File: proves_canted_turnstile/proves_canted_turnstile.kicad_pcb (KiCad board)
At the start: 4 copper layers, 100 x 100 mm, 23 parts, among them J1 Conn_Coaxial, J2 Conn_02x02_Counter_Clockwise, U1 QBA-07+, U2 QBA-07+, U3 QBA-07+

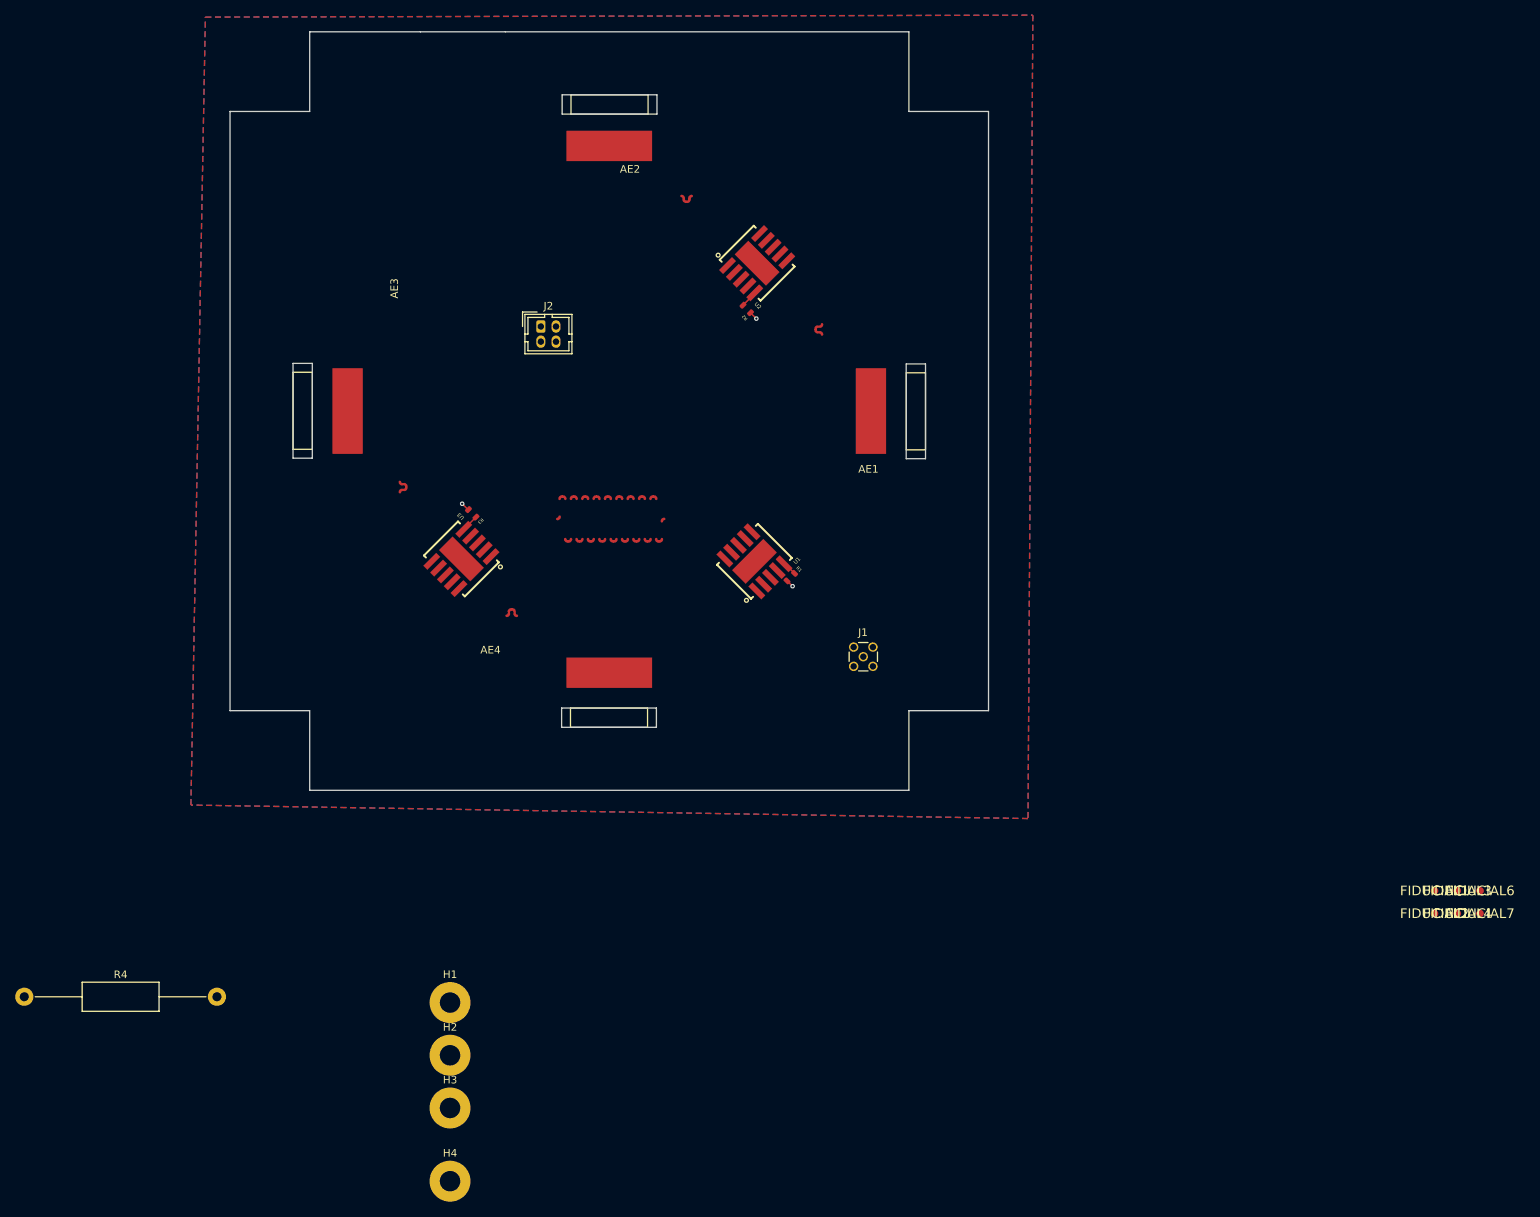
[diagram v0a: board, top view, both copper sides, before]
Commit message: placement of fiducials
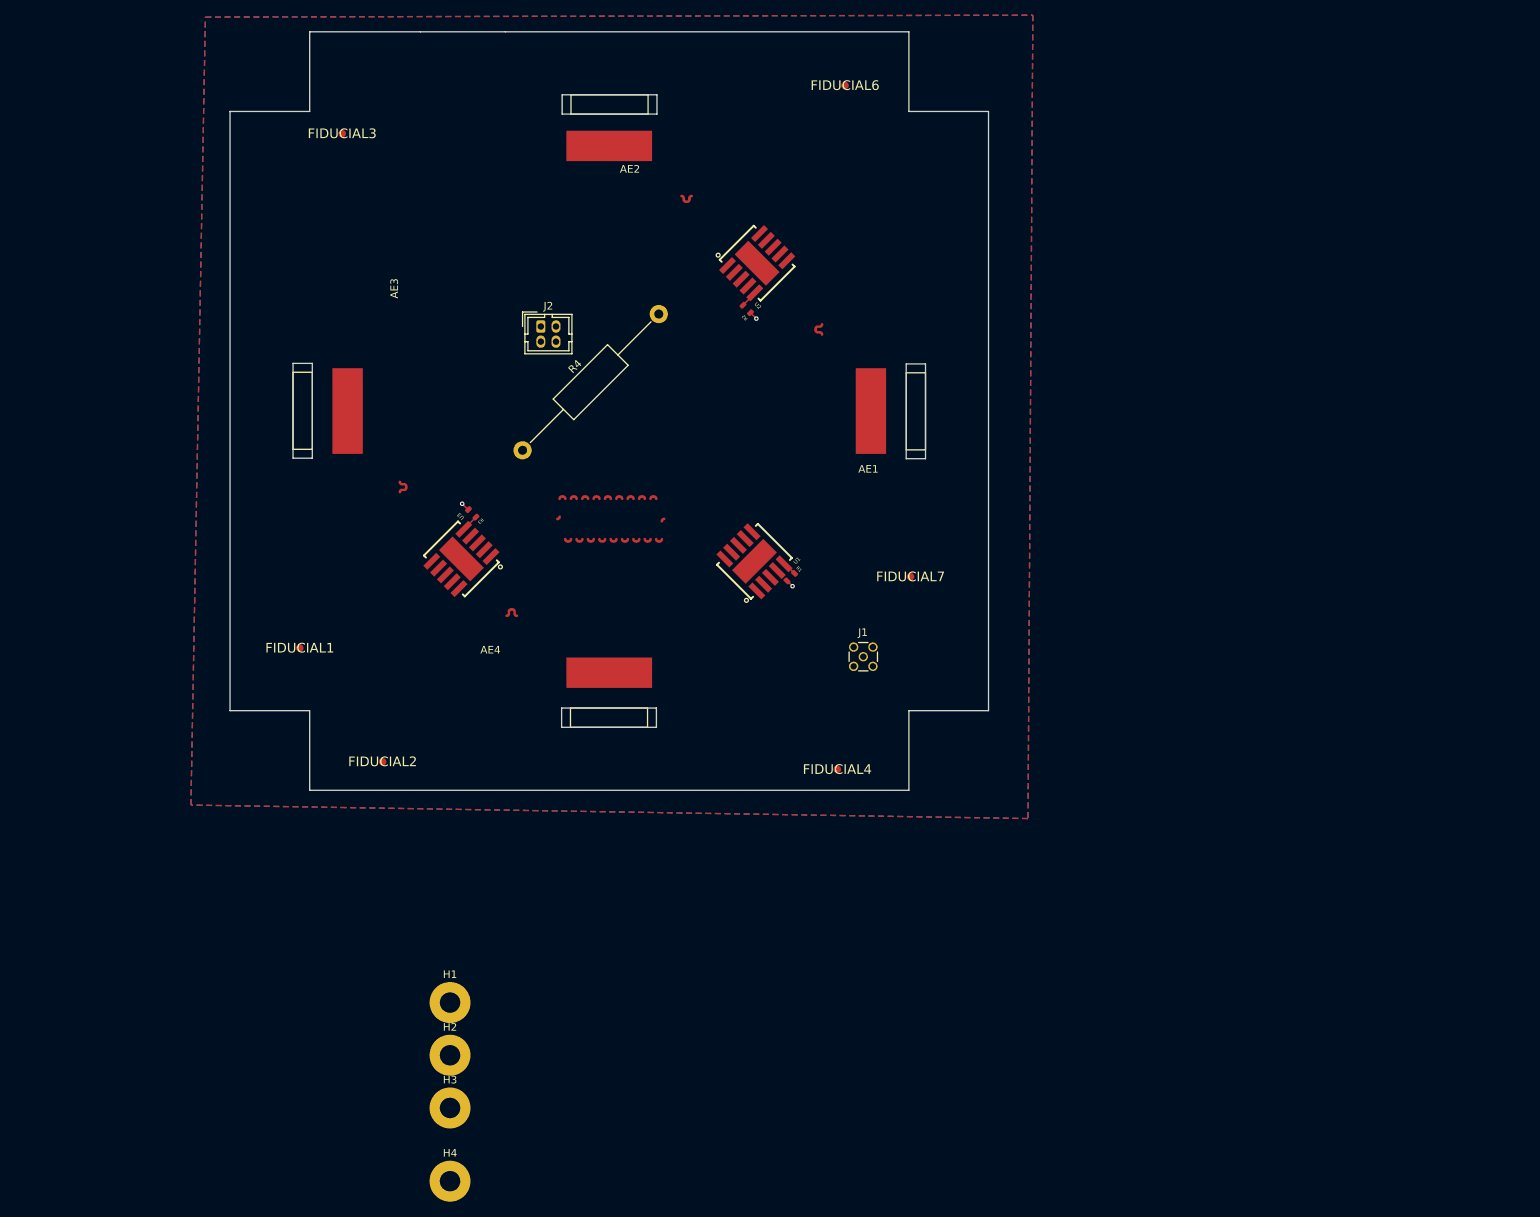
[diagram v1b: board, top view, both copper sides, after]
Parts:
- moved FIDUCIAL3 177.7 mm to (108.5, 46.0)
- moved FIDUCIAL1 153.0 mm to (102.9, 113.8)
- moved FIDUCIAL2 140.1 mm to (113.8, 128.8)
- moved FIDUCIAL6 135.2 mm to (174.8, 39.6)
- moved R4 97.5 mm to (132.2, 87.7), turned to 45 degrees
- moved FIDUCIAL7 87.2 mm to (183.4, 104.4)
- moved FIDUCIAL4 83.9 mm to (173.7, 129.8)
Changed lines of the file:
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@@
 	(footprint "plusz-end-card-with-turnstile-mezzanine-eagle-import:FIDUCIAL-1.0X2.0"
 		(layer "F.Cu")
-		(at 252.476 148.796)
+		(at 113.792 128.778)
 		(descr "Moderate Fiducial, 1.0 mm diameter with 2 mm mask clearance")
 		(property "Reference" "FIDUCIAL2"
@@
 	(footprint "plusz-end-card-with-turnstile-mezzanine-eagle-import:FIDUCIAL-1.0X2.0"
 		(layer "F.Cu")
-		(at 252.476 145.796)
+		(at 102.87 113.792)
 		(descr "Moderate Fiducial, 1.0 mm diameter with 2 mm mask clearance")
 		(property "Reference" "FIDUCIAL1"
@@
 	(footprint "plusz-end-card-with-turnstile-mezzanine-eagle-import:FIDUCIAL-1.0X2.0"
 		(layer "F.Cu")
-		(at 258.476 145.796)
+		(at 174.752 39.624)
 		(descr "Moderate Fiducial, 1.0 mm diameter with 2 mm mask clearance")
 		(property "Reference" "FIDUCIAL6"
@@
 	(footprint "plusz-end-card-with-turnstile-mezzanine-eagle-import:FIDUCIAL-1.0X2.0"
 		(layer "F.Cu")
-		(at 255.476 148.796)
+		(at 173.736 129.794)
 		(descr "Moderate Fiducial, 1.0 mm diameter with 2 mm mask clearance")
 		(property "Reference" "FIDUCIAL4"
@@
 	(footprint "plusz-end-card-with-turnstile-mezzanine-eagle-import:FIDUCIAL-1.0X2.0"
 		(layer "F.Cu")
-		(at 255.476 145.796)
+		(at 108.458 45.974)
 		(descr "Moderate Fiducial, 1.0 mm diameter with 2 mm mask clearance")
 		(property "Reference" "FIDUCIAL3"
@@
 	(footprint "plusz-end-card-with-turnstile-mezzanine-eagle-import:FIDUCIAL-1.0X2.0"
 		(layer "F.Cu")
-		(at 258.476 148.796)
+		(at 183.388 104.394)
 		(descr "Moderate Fiducial, 1.0 mm diameter with 2 mm mask clearance")
 		(property "Reference" "FIDUCIAL7"
@@
 	(footprint "Resistor_THT:R_Axial_DIN0411_L9.9mm_D3.6mm_P25.40mm_Horizontal"
 		(layer "F.Cu")
-		(at 66.548 159.766)
+		(at 132.243744 87.720256 45)
 		(descr "Resistor, Axial_DIN0411 series, Axial, Horizontal, pin pitch=25.4mm, 1W, length*diameter=9.9*3.6mm^2")
 		(tags "Resistor Axial_DIN0411 series Axial Horizontal pin pitch 25.4mm 1W length 9.9mm diameter 3.6mm")
 		(property "Reference" "R4"
-			(at 12.7 -2.92 0)
+			(at 12.7 -2.92 45)
 			(layer "F.SilkS")
 			(effects
@@
 		)
 		(property "Value" "R_Small_US"
-			(at 12.7 2.92 0)
+			(at 12.7 2.92 45)
 			(layer "F.Fab")
 			(effects
@@
 		)
 		(property "Datasheet" ""
-			(at 0 0 0)
+			(at 0 0 45)
 			(unlocked yes)
 			(layer "F.Fab")
@@
 		)
 		(property "Description" "Resistor, small US symbol"
-			(at 0 0 0)
+			(at 0 0 45)
 			(unlocked yes)
 			(layer "F.Fab")
@@
 		(fp_line
 			(start 7.63 1.92)
-			(end 17.77 1.92)
+			(end 17.77 1.920001)
 			(stroke
 				(width 0.12)
@@
 		)
 		(fp_line
-			(start 17.77 -1.92)
+			(start 17.77 -1.920001)
 			(end 7.63 -1.92)
 			(stroke
@@
 		)
 		(fp_line
-			(start 17.77 1.92)
-			(end 17.77 -1.92)
+			(start 17.77 1.920001)
+			(end 17.77 -1.920001)
 			(stroke
 				(width 0.12)
@@
 		)
 		(fp_line
-			(start 23.96 0)
-			(end 17.77 0)
+			(start 23.959999 0)
+			(end 17.770001 0)
 			(stroke
 				(width 0.12)
@@
 		(fp_line
 			(start 0 0)
-			(end 7.75 0)
+			(end 7.750001 0)
 			(stroke
 				(width 0.1)
@@
 		)
 		(fp_text user "${REFERENCE}"
-			(at 12.7 0 0)
+			(at 12.7 0 45)
 			(layer "F.Fab")
 			(effects
@@
 		)
 		(pad "1" thru_hole circle
-			(at 0 0)
+			(at 0 0 45)
 			(size 2.4 2.4)
 			(drill 1.2)
@@
 		)
 		(pad "2" thru_hole oval
-			(at 25.4 0)
+			(at 25.4 0 45)
 			(size 2.4 2.4)
 			(drill 1.2)

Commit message: placed mounting holes
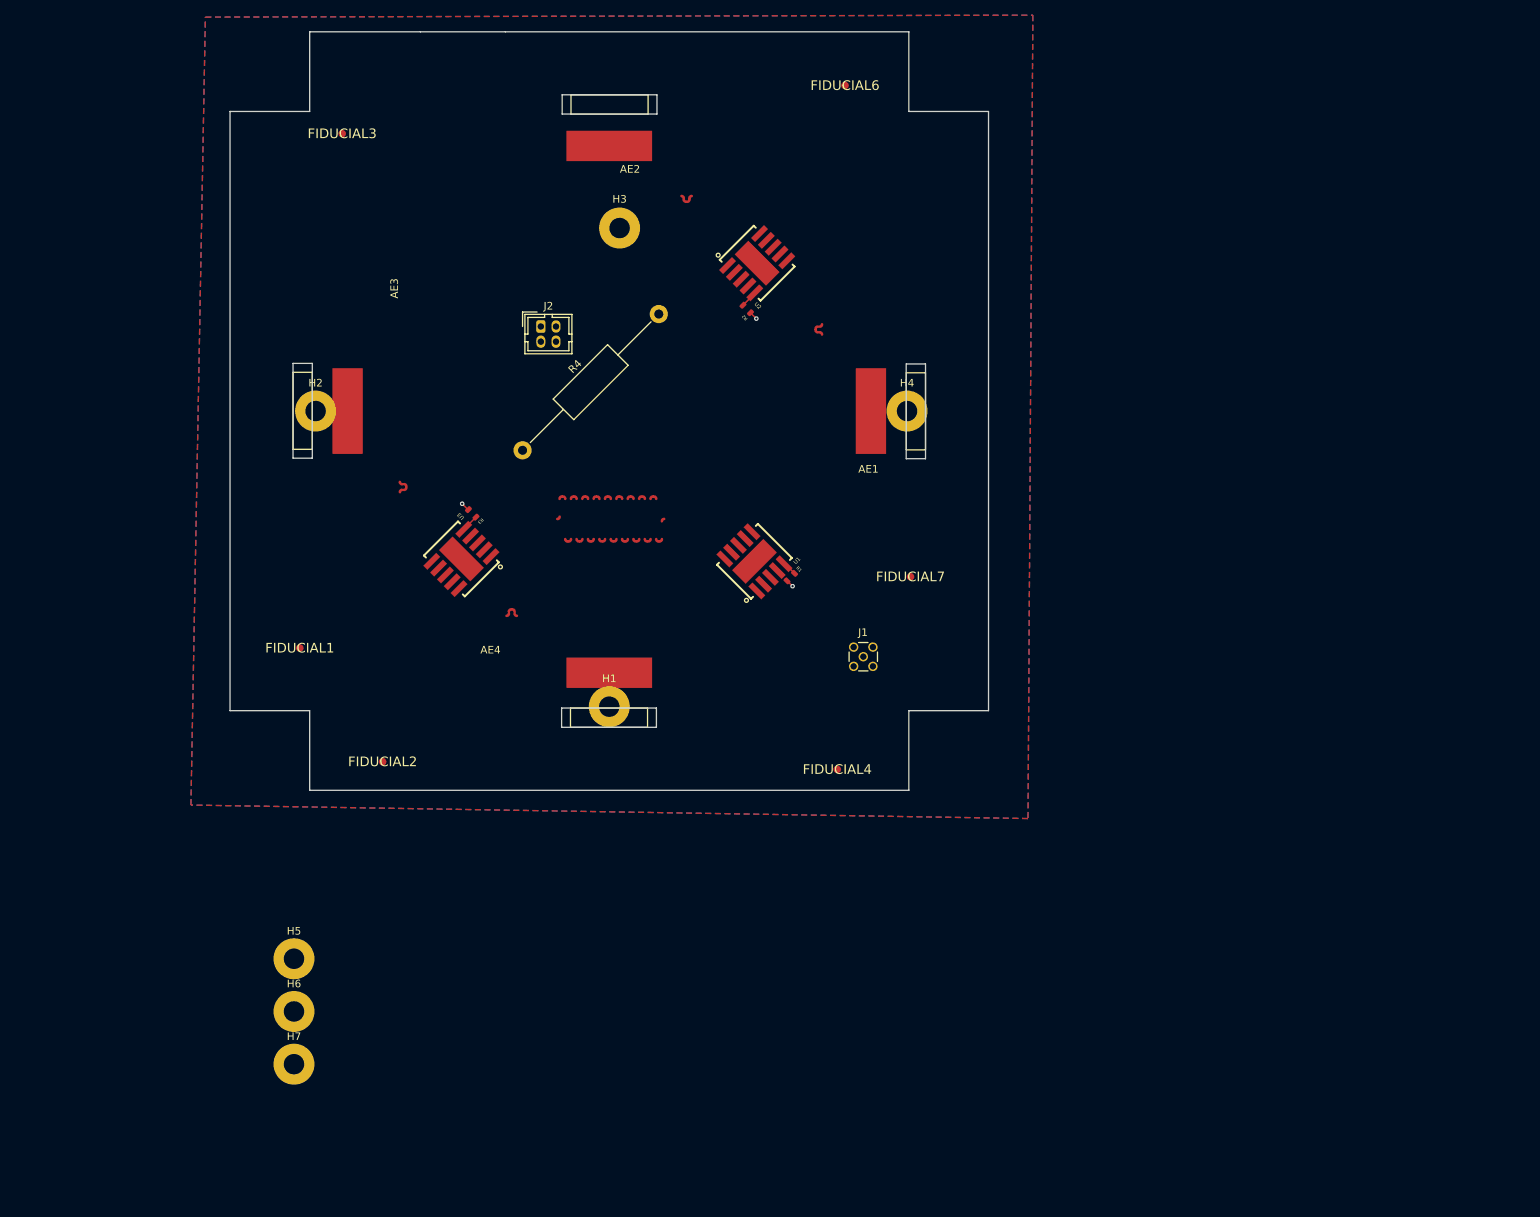
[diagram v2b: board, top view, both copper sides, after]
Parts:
- added H5: MountingHole, MountingHole:MountingHole_2.7mm_M2.5_Pad, F.Cu at (102.1, 154.8)
- added H6: MountingHole, MountingHole:MountingHole_2.7mm_M2.5_Pad, F.Cu at (102.1, 161.7)
- added H7: MountingHole, MountingHole:MountingHole_2.7mm_M2.5_Pad, F.Cu at (102.1, 168.7)
- moved H3 118.1 mm to (145.0, 58.4)
- moved H4 118.1 mm to (182.9, 82.5)
- moved H2 86.8 mm to (105.0, 82.5)
- moved H1 44.3 mm to (143.7, 121.5)

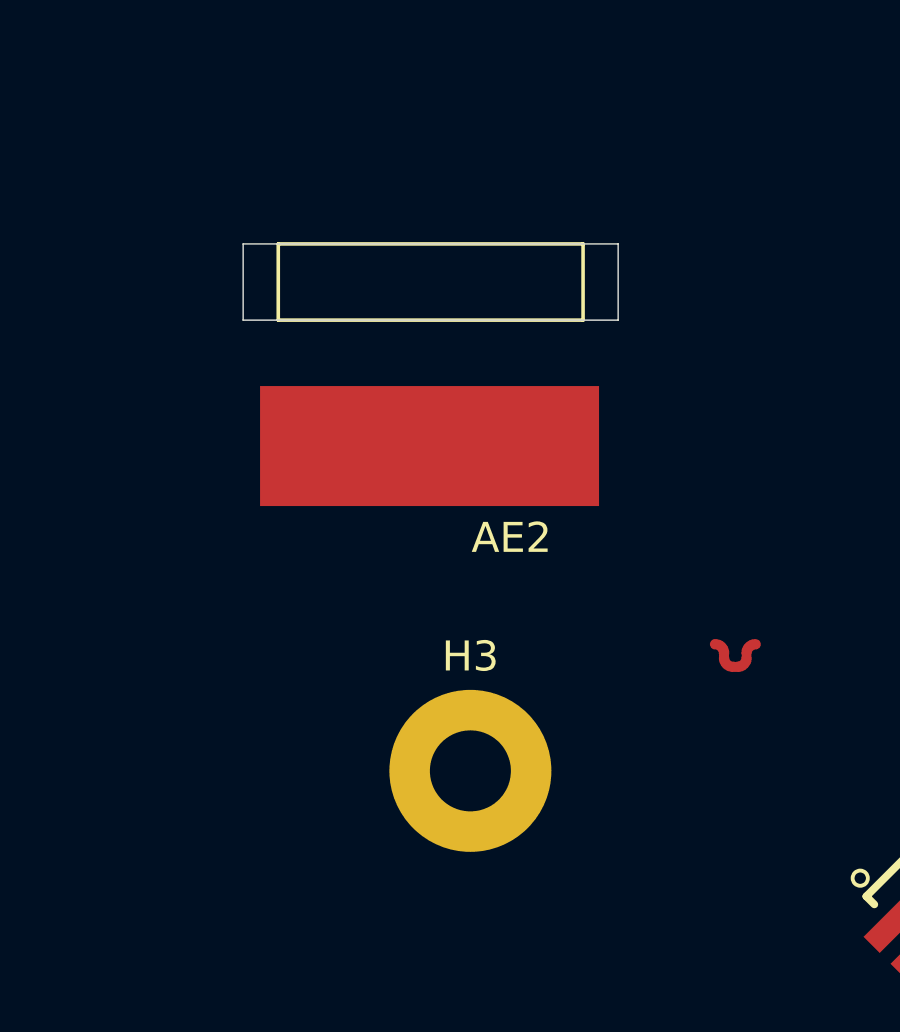
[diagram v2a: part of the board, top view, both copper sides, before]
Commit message: placed mounting holes
have to readjust the pads now : (
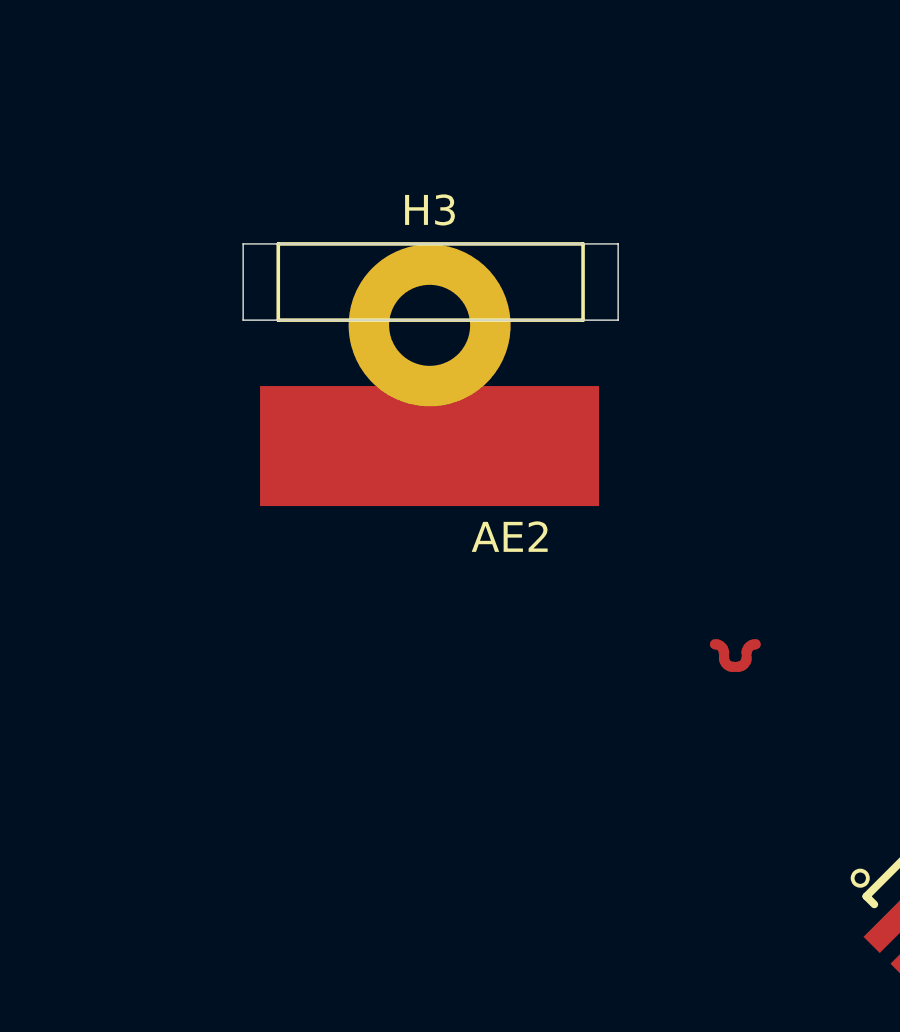
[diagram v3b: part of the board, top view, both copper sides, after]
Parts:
- moved H3 14.9 mm to (143.7, 43.6)
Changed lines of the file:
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@@
 	(footprint "MountingHole:MountingHole_2.7mm_M2.5_Pad"
 		(layer "F.Cu")
-		(at 145.034 58.42)
+		(at 143.675 43.5692)
 		(descr "Mounting Hole 2.7mm, M2.5")
 		(tags "mounting hole 2.7mm m2.5")
